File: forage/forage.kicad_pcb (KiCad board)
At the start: 2 copper layers, 308 x 79.4 mm, 69 parts, among them J1 Conn_01x04_MountingPin, Q1 AO3400A, U1 STM32G431RBTx, U2 XC6206P322MR

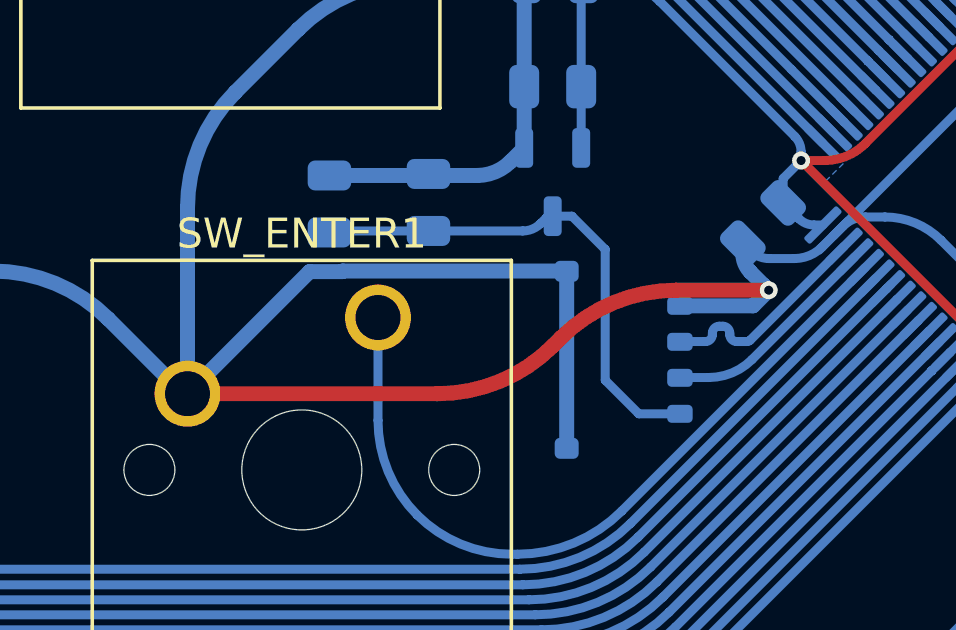
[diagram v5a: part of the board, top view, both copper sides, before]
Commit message: make the traces round too
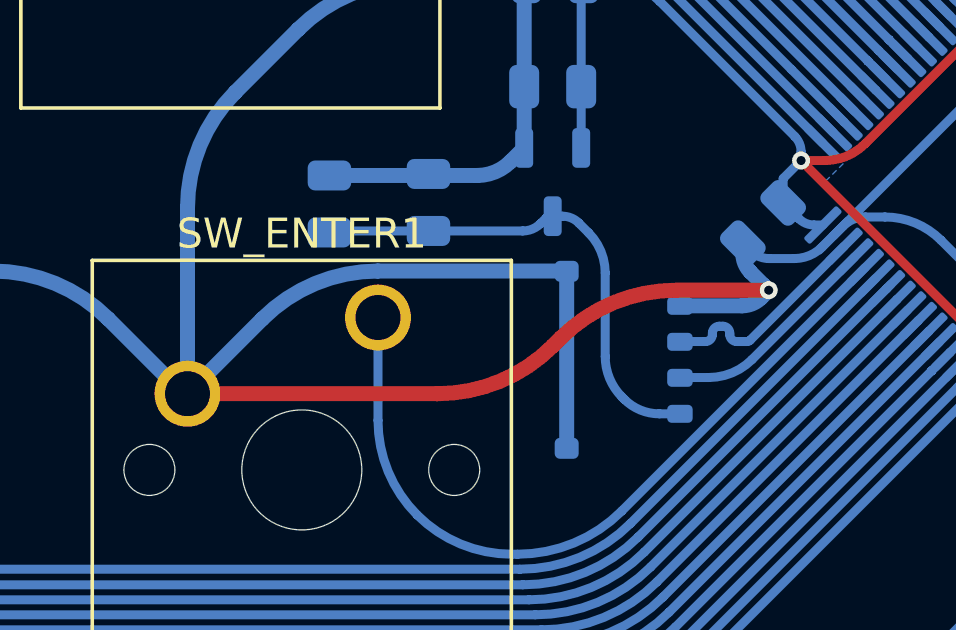
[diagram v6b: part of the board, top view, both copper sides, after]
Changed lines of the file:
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@@
 		(tags "connector Molex Pico-EZmate side entry")
 		(property "Reference" "J1"
-			(at -4.64 -0.025724 360)
+			(at -4.64 -0.025724 0)
 			(layer "B.SilkS")
 			(effects
@@
 		)
 		(property "Value" "Conn_01x04_MountingPin"
-			(at 0 -3.72 270)
+			(at 0 -3.72 -90)
 			(layer "B.Fab")
 			(effects
@@
 		)
 		(fp_text user "${REFERENCE}"
-			(at 0 -0.27 270)
+			(at 0 -0.27 -90)
 			(layer "B.Fab")
 			(effects
@@
 	)
 	(segment
-		(start 297.560724 146.93)
-		(end 300 146.93)
+		(start 299.632304 146.93)
+		(end 297.560724 146.93)
 		(width 0.5)
 		(layer "B.Cu")
@@
 	)
 	(segment
-		(start 293.775724 145.77)
-		(end 293.785724 145.78)
-		(width 0.5)
-		(layer "B.Cu")
-		(net 1)
-	)
-	(segment
 		(start 325.8179 136.4044)
 		(end 325.8058 136.3923)
@@
 	)
 	(segment
-		(start 300 146.93)
+		(start 300.26 146.67)
 		(end 300.52 146.41)
 		(width 0.5)
@@
 	)
 	(segment
-		(start 285.21625 145.79)
-		(end 286.3 145.79)
-		(width 0.5)
-		(layer "B.Cu")
-		(net 1)
-	)
-	(segment
 		(start 257.218792 147.363792)
 		(end 259.715 149.86)
@@
 	)
 	(segment
-		(start 286.32 145.77)
-		(end 293.775724 145.77)
-		(width 0.5)
-		(layer "B.Cu")
-		(net 1)
-	)
-	(segment
 		(start 300.533002 145.354804)
 		(end 301.374015 145.354804)
@@
 	)
 	(segment
+		(start 287.490213 145.77)
+		(end 293.768652 145.77)
+		(width 0.5)
+		(layer "B.Cu")
+		(net 1)
+	)
+	(segment
 		(start 228.643792 109.263792)
 		(end 231.14 111.76)
@@
 	)
 	(segment
+		(start 283.642457 147.363792)
+		(end 281.14625 149.86)
+		(width 0.5)
+		(layer "B.Cu")
+		(net 1)
+	)
+	(segment
 		(start 114.343792 109.263792)
 		(end 116.84 111.76)
@@
 	)
 	(segment
-		(start 281.14625 149.86)
-		(end 285.21625 145.79)
-		(width 0.5)
-		(layer "B.Cu")
-		(net 1)
-	)
-	(segment
 		(start 186.011207 147.363792)
 		(end 183.515 149.86)
@@
 	)
 	(segment
+		(start 293.780724 145.775)
+		(end 293.785724 145.78)
+		(width 0.5)
+		(layer "B.Cu")
+		(net 1)
+	)
+	(segment
 		(start 123.868792 147.363792)
 		(end 126.365 149.86)
@@
 		(net 1)
 	)
-	(segment
-		(start 286.3 145.79)
-		(end 286.32 145.77)
-		(width 0.5)
-		(layer "B.Cu")
-		(net 1)
-	)
 	(arc
 		(start 273.887542 109.263792)
@@
 	)
 	(arc
+		(start 300.26 146.67)
+		(mid 299.97201 146.862428)
+		(end 299.632304 146.93)
+		(width 0.5)
+		(layer "B.Cu")
+		(net 1)
+	)
+	(arc
 		(start 64.61125 150.01875)
 		(mid 64.728742 150.194589)
@@
 	)
 	(arc
+		(start 287.490213 145.77)
+		(mid 285.407822 146.184213)
+		(end 283.642457 147.363792)
+		(width 0.5)
+		(layer "B.Cu")
+		(net 1)
+	)
+	(arc
 		(start 142.918792 147.363792)
 		(mid 141.153426 146.184213)
@@
 	)
 	(arc
+		(start 293.780724 145.775)
+		(mid 293.775185 145.771299)
+		(end 293.768652 145.77)
+		(width 0.5)
+		(layer "B.Cu")
+		(net 1)
+	)
+	(arc
 		(start 280.948292 149.808292)
 		(mid 281.005566 149.846561)
@@
 	)
 	(segment
-		(start 293.9618 143.9418)
-		(end 295.07 145.05)
+		(start 294.188993 144.168993)
+		(end 294.5159 144.4959)
 		(width 0.3)
 		(layer "B.Cu")
@@
 	)
 	(segment
-		(start 296.19 150.53)
+		(start 296.875362 150.53)
 		(end 297.560724 150.53)
 		(width 0.3)
@@
 	)
 	(segment
-		(start 295.07 149.41)
-		(end 296.19 150.53)
+		(start 295.705375 150.045375)
+		(end 295.63 149.97)
 		(width 0.3)
 		(layer "B.Cu")
@@
 	)
 	(segment
-		(start 293.3192 143.9418)
-		(end 293.9618 143.9418)
+		(start 293.6405 143.9418)
+		(end 293.3192 143.9418)
 		(width 0.3)
 		(layer "B.Cu")
@@
 	)
 	(segment
-		(start 295.07 145.05)
-		(end 295.07 149.41)
+		(start 295.07 145.833615)
+		(end 295.07 148.61804)
+		(width 0.3)
+		(layer "B.Cu")
+		(net 4)
+	)
+	(arc
+		(start 294.188993 144.168993)
+		(mid 293.937342 144.000845)
+		(end 293.6405 143.9418)
+		(width 0.3)
+		(layer "B.Cu")
+		(net 4)
+	)
+	(arc
+		(start 295.07 148.61804)
+		(mid 295.215539 149.349715)
+		(end 295.63 149.97)
 		(width 0.3)
 		(layer "B.Cu")
@@
 	)
 	(arc
+		(start 294.5159 144.4959)
+		(mid 294.925994 145.109649)
+		(end 295.07 145.833615)
+		(width 0.3)
+		(layer "B.Cu")
+		(net 4)
+	)
+	(arc
 		(start 293.2405 143.9418)
 		(mid 293.16779 143.956262)
@@
 		(width 0.3)
 		(layer "B.Cu")
+		(net 4)
+	)
+	(arc
+		(start 295.705375 150.045375)
+		(mid 296.242169 150.40405)
+		(end 296.875362 150.53)
+		(width 0.3)
+		(layer "B.Cu")

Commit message: move some ground traces to the other side
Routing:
- net GND: track 1333.6 -> 1262.0 mm

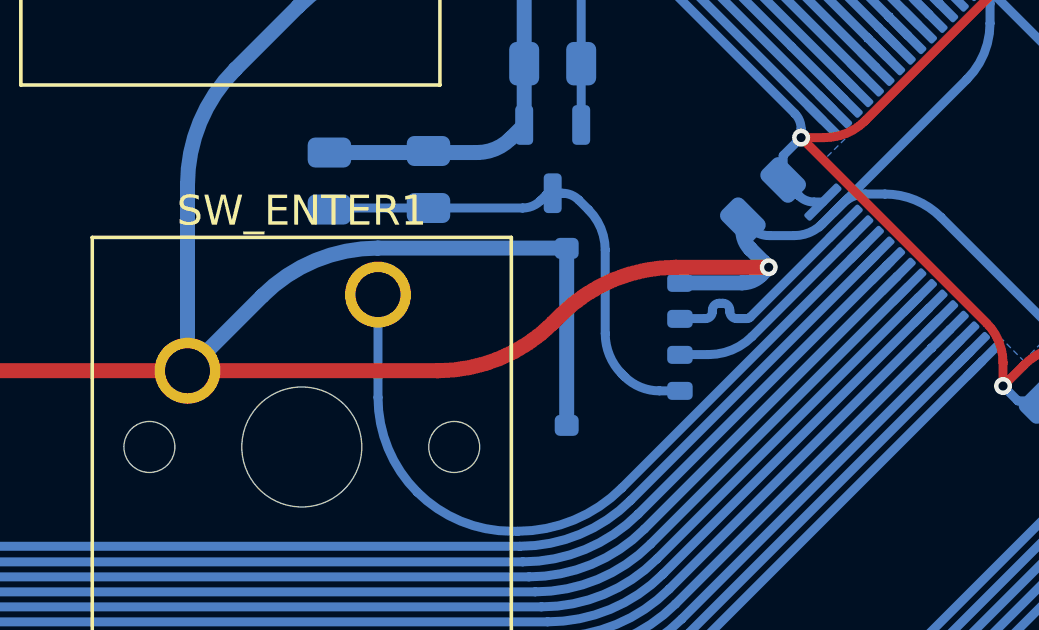
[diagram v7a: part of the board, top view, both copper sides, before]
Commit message: switch to jst
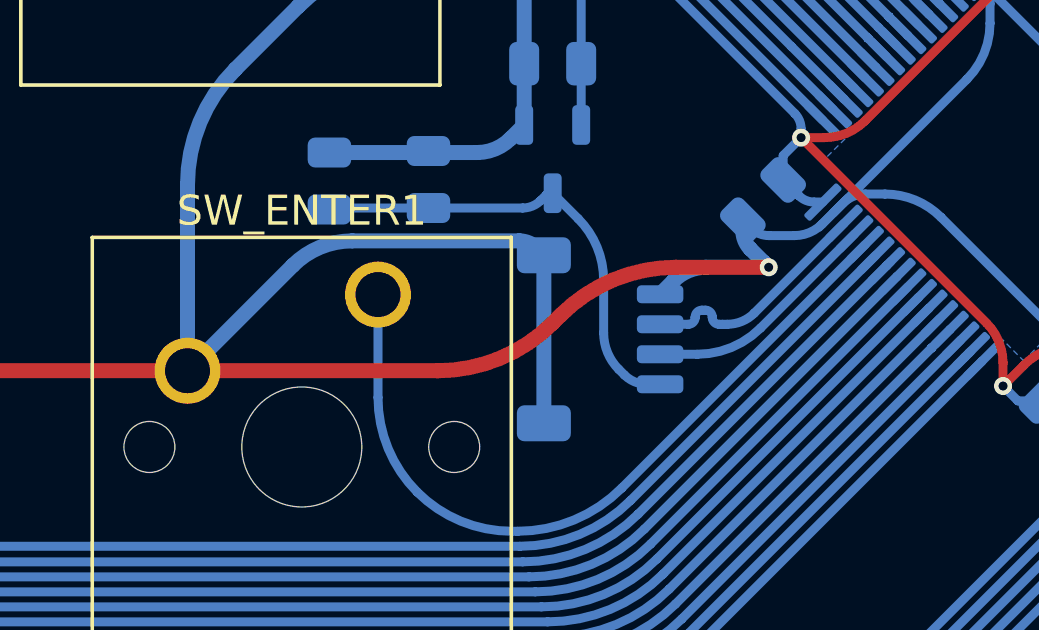
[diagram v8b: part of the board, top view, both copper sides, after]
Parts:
- J1: footprint Connector_Molex:Molex_Pico-EZmate_78171-0004_1x04-1MP_P1.20mm_Vertical -> Connector_JST:JST_SH_SM04B-SRSS-TB_1x04-1MP_P1.00mm_Horizontal
- moved J1 0.79 mm to (294.9, 148.8)
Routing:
- net +5V: track 16.8 -> 15.7 mm
- net D+: track 7.30 -> 8.01 mm
- net D-: track 7.30 -> 8.01 mm
